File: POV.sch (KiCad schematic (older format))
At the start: 14 parts, among them IC1 ATTINY85-P, SW1 SPDT

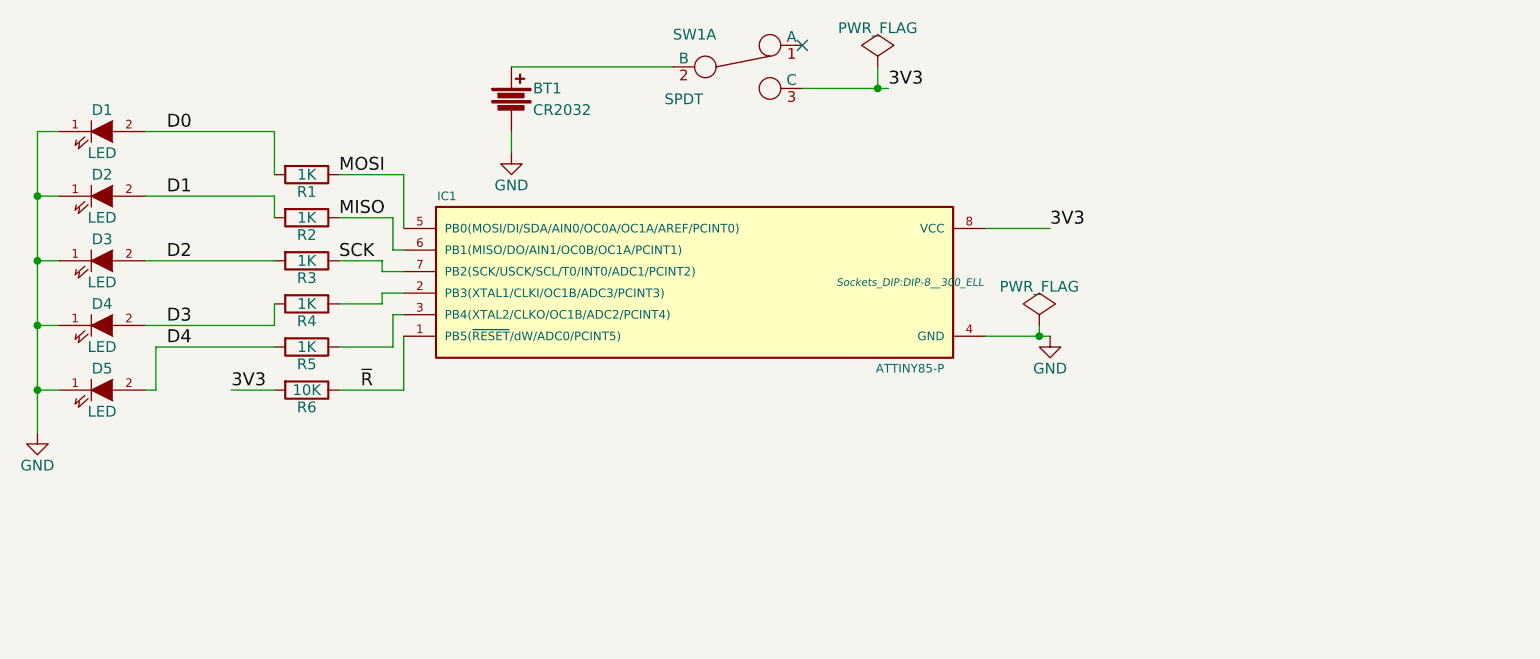
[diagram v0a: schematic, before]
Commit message: Added gerbers, updated FP,added logos
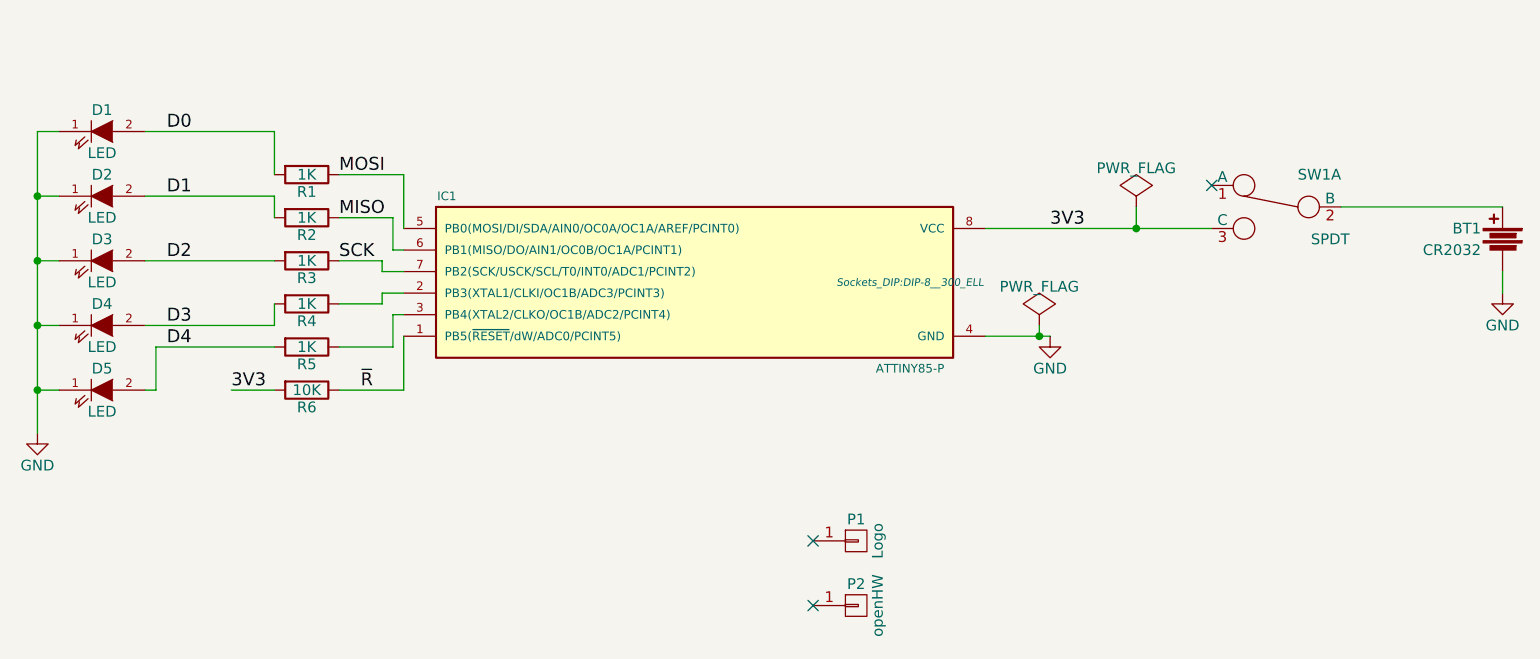
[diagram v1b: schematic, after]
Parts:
- added P1: Logo, logo:3k5, symbol CONN_01X01
- added P2: openHW, logo:oshw-logo-kicad-copper-10mm, symbol CONN_01X01
- BT1: footprint terminal:CR2032 -> terminal:CR2032H
- R1, R2, R3, R4, R5: footprint Resistors_ThroughHole:Resistor_Vertical_RM5mm -> Resistors_ThroughHole:Resistor_Horizontal_RM10mm
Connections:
- no-connect marks 1 -> 3
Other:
- moved on the sheet: BT1, SW1A
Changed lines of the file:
@@
 F 0 "R1" V 2880 2000 50  0000 C CNN
 F 1 "1K" V 2800 2000 50  0000 C CNN
-F 2 "Resistors_ThroughHole:Resistor_Vertical_RM5mm" V 2730 2000 30  0001 C CNN
+F 2 "Resistors_ThroughHole:Resistor_Horizontal_RM10mm" V 2730 2000 30  0001 C CNN
 F 3 "" H 2800 2000 30  0000 C CNN
 	1    2800 2000
@@
 F 0 "R2" V 2880 2200 50  0000 C CNN
 F 1 "1K" V 2800 2200 50  0000 C CNN
-F 2 "Resistors_ThroughHole:Resistor_Vertical_RM5mm" V 2730 2200 30  0001 C CNN
+F 2 "Resistors_ThroughHole:Resistor_Horizontal_RM10mm" V 2730 2200 30  0001 C CNN
 F 3 "" H 2800 2200 30  0000 C CNN
 	1    2800 2200
@@
 F 0 "R3" V 2880 2400 50  0000 C CNN
 F 1 "1K" V 2800 2400 50  0000 C CNN
-F 2 "Resistors_ThroughHole:Resistor_Vertical_RM5mm" V 2730 2400 30  0001 C CNN
+F 2 "Resistors_ThroughHole:Resistor_Horizontal_RM10mm" V 2730 2400 30  0001 C CNN
 F 3 "" H 2800 2400 30  0000 C CNN
 	1    2800 2400
@@
 F 0 "R4" V 2880 2600 50  0000 C CNN
 F 1 "1K" V 2800 2600 50  0000 C CNN
-F 2 "Resistors_ThroughHole:Resistor_Vertical_RM5mm" V 2730 2600 30  0001 C CNN
+F 2 "Resistors_ThroughHole:Resistor_Horizontal_RM10mm" V 2730 2600 30  0001 C CNN
 F 3 "" H 2800 2600 30  0000 C CNN
 	1    2800 2600
@@
 F 0 "R5" V 2880 2800 50  0000 C CNN
 F 1 "1K" V 2800 2800 50  0000 C CNN
-F 2 "Resistors_ThroughHole:Resistor_Vertical_RM5mm" V 2730 2800 30  0001 C CNN
+F 2 "Resistors_ThroughHole:Resistor_Horizontal_RM10mm" V 2730 2800 30  0001 C CNN
 F 3 "" H 2800 2800 30  0000 C CNN
 	1    2800 2800
@@
 L Switch_SPDT_x2 SW1
 U 1 1 560BB533
-P 4800 1500
-F 0 "SW1" H 4600 1650 50  0000 C CNN
-F 1 "SPDT" H 4550 1350 50  0000 C CNN
-F 2 "Buttons_Switches_ThroughHole:SW_Micro_SPST" H 4800 1500 60  0001 C CNN
-F 3 "" H 4800 1500 60  0000 C CNN
-	1    4800 1500
-	1    0    0    -1
+P 7300 2150
+F 0 "SW1" H 7100 2300 50  0000 C CNN
+F 1 "SPDT" H 7050 2000 50  0000 C CNN
+F 2 "Buttons_Switches_ThroughHole:SW_Micro_SPST" H 7300 2150 60  0001 C CNN
+F 3 "" H 7300 2150 60  0000 C CNN
+	1    7300 2150
+	-1   0    0    -1
 $EndComp
 $Comp
 L Battery BT1
 U 1 1 560BB5DC
-P 3750 1650
-F 0 "BT1" H 3850 1700 50  0000 L CNN
-F 1 "CR2032" H 3850 1600 50  0000 L CNN
-F 2 "terminal:CR2032" V 3750 1690 60  0001 C CNN
-F 3 "" V 3750 1690 60  0000 C CNN
-	1    3750 1650
-	1    0    0    -1
+P 8350 2300
+F 0 "BT1" H 8450 2350 50  0000 L CNN
+F 1 "CR2032" H 8450 2250 50  0000 L CNN
+F 2 "terminal:CR2032H" V 8350 2340 60  0001 C CNN
+F 3 "" V 8350 2340 60  0000 C CNN
+	1    8350 2300
+	-1   0    0    -1
 $EndComp
 Wire Wire Line
@@
 	2450 3000 2650 3000
 Wire Wire Line
-	3750 1500 4500 1500
-Wire Wire Line
-	5100 1600 5500 1600
+	8350 2150 7600 2150
+Wire Wire Line
+	5950 2250 7000 2250
 $Comp
 L GND #PWR01
 U 1 1 560BC93F
-P 3750 1900
-F 0 "#PWR01" H 3750 1650 50  0001 C CNN
-F 1 "GND" H 3750 1750 50  0000 C CNN
-F 2 "" H 3750 1900 60  0000 C CNN
-F 3 "" H 3750 1900 60  0000 C CNN
-	1    3750 1900
-	1    0    0    -1
-$EndComp
-Wire Wire Line
-	3750 1800 3750 1900
-Text Label 5500 1600 0    60   ~ 0
-3V3
-Wire Wire Line
-	5950 2250 6250 2250
+P 8350 2550
+F 0 "#PWR01" H 8350 2300 50  0001 C CNN
+F 1 "GND" H 8350 2400 50  0000 C CNN
+F 2 "" H 8350 2550 60  0000 C CNN
+F 3 "" H 8350 2550 60  0000 C CNN
+	1    8350 2550
+	-1   0    0    -1
+$EndComp
+Wire Wire Line
+	8350 2450 8350 2550
 Wire Wire Line
 	5950 2750 6250 2750
@@
 	2100 2800 2650 2800
 $Comp
-L GND #PWR04
+L GND #PWR03
 U 1 1 560BEC50
 P 1550 3200
-F 0 "#PWR04" H 1550 2950 50  0001 C CNN
+F 0 "#PWR03" H 1550 2950 50  0001 C CNN
 F 1 "GND" H 1550 3050 50  0000 C CNN
 F 2 "" H 1550 3200 60  0000 C CNN
@@
 Text Label 2150 2800 0    60   ~ 0
 D4
-NoConn ~ 5100 1400
+NoConn ~ 7000 2050
+$Comp
+L PWR_FLAG #FLG04
+U 1 1 560C1096
+P 6650 2150
+F 0 "#FLG04" H 6650 2245 50  0001 C CNN
+F 1 "PWR_FLAG" H 6650 2330 50  0000 C CNN
+F 2 "" H 6650 2150 60  0000 C CNN
+F 3 "" H 6650 2150 60  0000 C CNN
+	1    6650 2150
+	-1   0    0    -1
+$EndComp
+Wire Wire Line
+	6650 2150 6650 2250
+Connection ~ 6650 2250
 $Comp
 L PWR_FLAG #FLG05
-U 1 1 560C1096
-P 5450 1500
-F 0 "#FLG05" H 5450 1595 50  0001 C CNN
-F 1 "PWR_FLAG" H 5450 1680 50  0000 C CNN
-F 2 "" H 5450 1500 60  0000 C CNN
-F 3 "" H 5450 1500 60  0000 C CNN
-	1    5450 1500
-	1    0    0    -1
-$EndComp
-Wire Wire Line
-	5450 1500 5450 1600
-Connection ~ 5450 1600
-$Comp
-L PWR_FLAG #FLG06
 U 1 1 560C1207
 P 6200 2700
-F 0 "#FLG06" H 6200 2795 50  0001 C CNN
+F 0 "#FLG05" H 6200 2795 50  0001 C CNN
 F 1 "PWR_FLAG" H 6200 2880 50  0000 C CNN
 F 2 "" H 6200 2700 60  0000 C CNN
@@
 	6200 2700 6200 2750
 Connection ~ 6200 2750
+$Comp
+L CONN_01X01 P1
+U 1 1 58147508
+P 5350 3700
+F 0 "P1" H 5350 3800 50  0000 C CNN
+F 1 "Logo" V 5450 3700 50  0000 C CNN
+F 2 "logo:3k5" H 5350 3700 50  0001 C CNN
+F 3 "" H 5350 3700 50  0000 C CNN
+	1    5350 3700
+	1    0    0    -1
+$EndComp
+NoConn ~ 5150 3700
+$Comp
+L CONN_01X01 P2
+U 1 1 581476CC
+P 5350 4000
+F 0 "P2" H 5350 4100 50  0000 C CNN
+F 1 "openHW" V 5450 4000 50  0000 C CNN
+F 2 "logo:oshw-logo-kicad-copper-10mm" H 5350 4000 50  0001 C CNN
+F 3 "" H 5350 4000 50  0000 C CNN
+	1    5350 4000
+	1    0    0    -1
+$EndComp
+NoConn ~ 5150 4000
 $EndSCHEMATC
